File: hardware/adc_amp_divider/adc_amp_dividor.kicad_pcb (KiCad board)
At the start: 2 copper layers, 40 x 80 mm, 86 parts, among them M1 CONN_1, M2 CONN_1, P1 CONN_10X2, P2 CONN_4, P3 CONN_6, P4 CONN_3, U1 OP2340, U2 OP2340, U3 OP2340, U4 OP2340, U5 OP2340

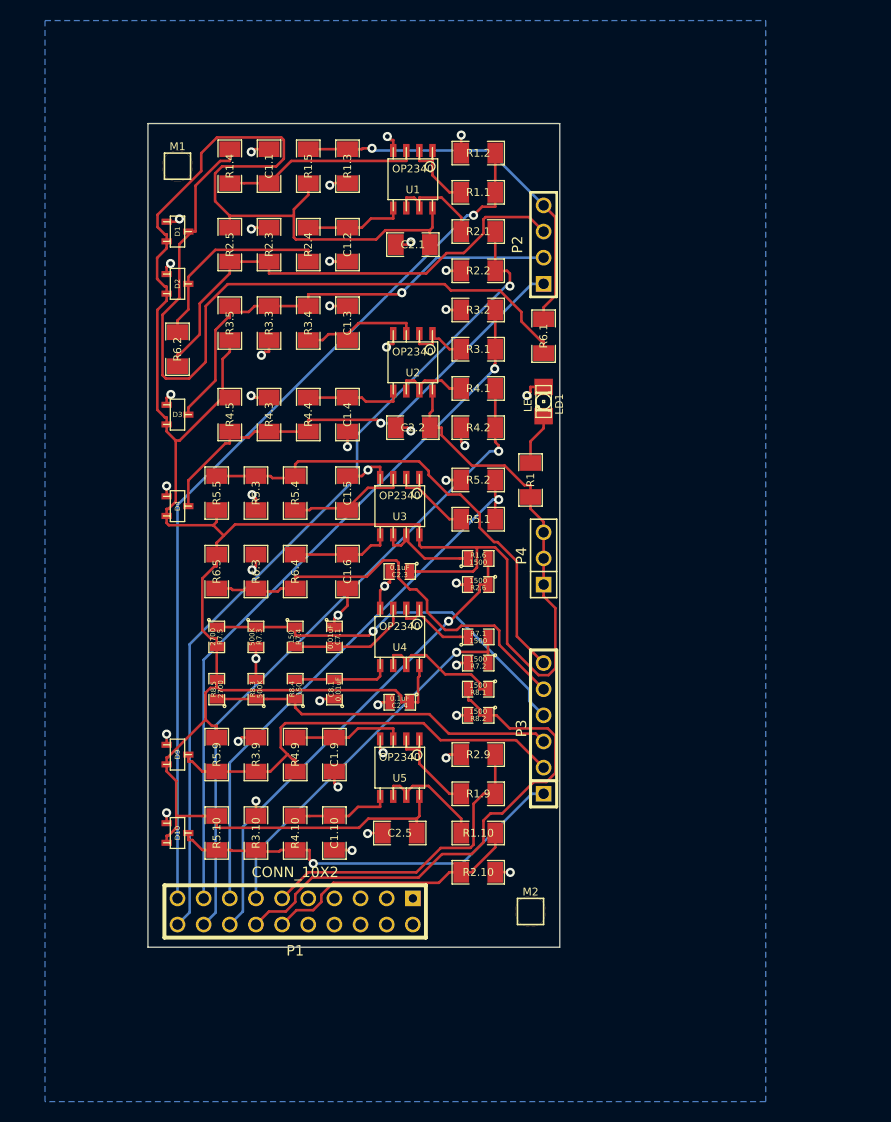
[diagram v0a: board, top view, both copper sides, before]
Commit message: now quad op-amps
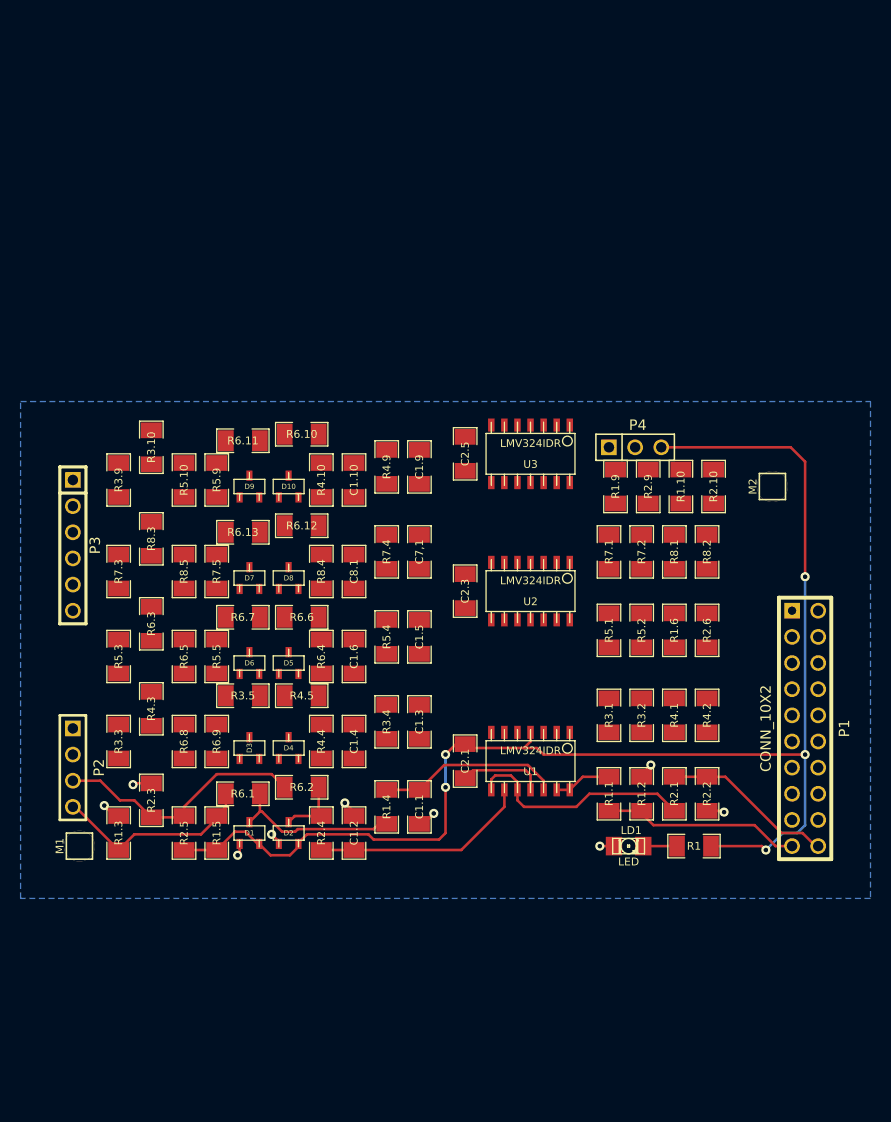
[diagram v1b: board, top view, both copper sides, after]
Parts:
- removed C2.2: 0.1uF, SM1206
- removed C2.4: 0.1uF, SM0805
- removed U4, U5: OP2340, so-8
- added D5: DOUBLE_SCHOTTKY, sot23, F.Cu at (113.7, 152.4)
- added D6: DOUBLE_SCHOTTKY, sot23, F.Cu at (109.9, 152.4)
- added D7: DOUBLE_SCHOTTKY, sot23, F.Cu at (109.9, 144.1)
- added D8: DOUBLE_SCHOTTKY, sot23, F.Cu at (113.7, 144.1)
- added R6.10: 10k, SM1206, F.Cu at (114.9, 130.2)
- added R6.11: 10k, SM1206, F.Cu at (109.2, 130.8)
- added R6.12: 10k, SM1206, F.Cu at (114.9, 139.1)
- added R6.13: 10k, SM1206, F.Cu at (109.2, 139.7)
- added R6.6: 10k, SM1206, F.Cu at (114.9, 148.0)
- added R6.7: 10k, SM1206, F.Cu at (109.2, 148.0)
- added R6.8: 10k, SM1206, F.Cu at (103.5, 160.0)
- added R6.9: 10k, SM1206, F.Cu at (106.7, 160.0)
- C2.3, C7,1, C8.1, R1.6, R2.6, R7.1, R7.2, R7.3, R7.4, R7.5, R8.1, R8.2, R8.3, R8.4, R8.5: footprint SM0805 -> SM1206
- U1, U2, U3: value OP2340 -> LMV324IDR; footprint so-8 -> so-14
- moved R1.3 68.5 mm to (97.2, 168.9), turned to 90 degrees
- moved P2 68.3 mm to (92.7, 162.6), turned to 270 degrees
- moved M1 66.7 mm to (93.3, 170.2), turned to 90 degrees
- moved R1.5 65.4 mm to (106.7, 168.9)
- moved R1.2 64.2 mm to (148.0, 165.1), turned to 90 degrees
- moved R1.4 64.1 mm to (123.2, 166.4), turned to 90 degrees
- moved C1.1 63.9 mm to (126.4, 166.4), turned to 90 degrees
- moved R1.1 59.8 mm to (144.8, 165.1), turned to 270 degrees
- moved D1 58.8 mm to (109.9, 168.9), turned to 0 degrees
- moved R2.1 57.8 mm to (151.1, 165.1), turned to 90 degrees
- moved U1 57.7 mm to (137.2, 161.9)
- moved R2.5 57.3 mm to (103.5, 168.9), turned to 270 degrees
- moved R2.4 57.2 mm to (116.8, 168.9), turned to 270 degrees
- moved C1.2 57.2 mm to (120.0, 168.9), turned to 270 degrees
- moved R2.2 55.4 mm to (154.3, 165.1), turned to 270 degrees
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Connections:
- C1.1 pad 2: N-0000042 -> N-0000064
- C1.10 pad 2: N-0000032 -> N-0000042
- C1.2 pad 2: N-0000040 -> N-0000062
- C1.3 pad 2: N-0000043 -> N-0000063
- C1.4 pad 2: N-0000063 -> N-0000066
- C1.5 pad 2: N-0000059 -> N-0000010
- C1.6 pad 2: N-0000060 -> N-0000011
- C1.9 pad 2: N-0000037 -> N-0000039
- C7,1 pad 2: N-0000064 -> N-0000035
- C8.1 pad 2: N-0000065 -> N-0000013
- D10 pad 2: /INP10 -> N-0000030
- D3 pad 2: /INP3 -> N-0000077
- D4 pad 2: /INP4 -> N-0000065
- D9 pad 2: /INP9 -> N-0000031
- P3 pad 5: /INP6 -> (no net)
- R1.1 pad 1: N-0000026 -> N-0000076
- R1.10 pad 1: N-0000031 -> N-000006
- R1.4 pad 2: N-0000042 -> N-0000064
- R1.6 pad 1: N-000003 -> N-0000015
- R1.9 pad 1: N-0000030 -> N-000001
- R2.1 pad 1: N-0000024 -> N-0000028
- R2.4 pad 2: N-0000040 -> N-0000062
- R3.1 pad 1: N-0000022 -> N-0000043
- R3.4 pad 1: /INP3 -> N-0000077
- R3.4 pad 2: N-0000043 -> N-0000063
- R4.1 pad 1: N-0000023 -> N-0000046
- R4.10 pad 1: /INP10 -> N-0000030
- R4.10 pad 2: N-0000032 -> N-0000042
- R4.4 pad 1: /INP4 -> N-0000065
- R4.4 pad 2: N-0000063 -> N-0000066
- R4.9 pad 1: /INP9 -> N-0000031
- R4.9 pad 2: N-0000037 -> N-0000039
- R5.1 pad 1: N-000002 -> N-0000012
- R5.4 pad 1: /INP5 -> N-0000054
- R5.4 pad 2: N-0000059 -> N-0000010
- R6.3 pad 1: /INP6 -> N-0000078
- R6.4 pad 1: /INP6 -> N-0000055
- R6.4 pad 2: N-0000060 -> N-0000011
- R6.5 pad 1: /INP6 -> N-0000078
- R7.1 pad 1: N-0000028 -> N-0000034
- R7.4 pad 1: /INP7 -> N-0000025
- R7.4 pad 2: N-0000064 -> N-0000035
- R8.1 pad 1: N-0000029 -> N-0000049
- R8.4 pad 1: /INP8 -> N-0000024
- R8.4 pad 2: N-0000065 -> N-0000013
- U1 pad 1: N-0000026 -> N-0000043
- U1 pad 2: N-0000026 -> N-0000043
- U1 pad 3: N-0000042 -> N-0000063
- U1 pad 4: GND -> VCC
- U1 pad 5: N-0000040 -> N-0000066
- U1 pad 6: N-0000024 -> N-0000046
- U1 pad 7: N-0000024 -> N-0000046
- U1 pad 8: VCC -> N-0000028
- U2 pad 1: N-0000022 -> N-0000034
- U2 pad 2: N-0000022 -> N-0000034
- U2 pad 3: N-0000043 -> N-0000035
- U2 pad 4: GND -> VCC
- U2 pad 5: N-0000063 -> N-0000013
- U2 pad 6: N-0000023 -> N-0000049
- U2 pad 7: N-0000023 -> N-0000049
- U2 pad 8: VCC -> N-0000015
- U3 pad 1: N-000002 -> (no net)
- U3 pad 2: N-000002 -> (no net)
- U3 pad 3: N-0000059 -> (no net)
- U3 pad 4: GND -> VCC
- U3 pad 5: N-0000060 -> (no net)
- U3 pad 6: N-000003 -> (no net)
- U3 pad 7: N-000003 -> (no net)
- U3 pad 8: VCC -> N-000006
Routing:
- net VCC: track 293.2 -> 134.0 mm, vias 0 -> 5
- net /OUT3: track 68.9 -> 0.00 mm, vias 1 -> 0
- net /OUT1: track 86.3 -> 19.3 mm, vias 1 -> 0
- net /OUT2: track 82.2 -> 16.8 mm, vias 1 -> 0
- net /OUT4: track 64.6 -> 0.00 mm, vias 1 -> 0
- net N-0000051: track 73.9 -> 16.6 mm
- net GND: track 76.7 -> 22.6 mm, vias 43 -> 9
- net /OUT5: track 54.0 -> 0.00 mm, vias 1 -> 0
- net /OUT8: track 51.8 -> 0.00 mm
- net /INP4: track 46.8 -> 0.00 mm, vias 1 -> 0
- net /INP5: track 46.7 -> 0.00 mm
- net /OUT6: track 46.5 -> 0.00 mm, vias 1 -> 0
- net /INP3: track 45.7 -> 0.00 mm, vias 1 -> 0
- net /INP9: track 43.9 -> 0.00 mm
- net /INP6: track 41.9 -> 0.00 mm
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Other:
- board outline removed
